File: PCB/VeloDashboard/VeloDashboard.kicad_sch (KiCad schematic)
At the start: 1 part

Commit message: Teensy & LDD & Led strips
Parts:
- added C1: 22nF, symbol Device:C_Polarized
- added IC1, IC2, IC3, IC4: LDD-700L, LDD-XXXL, symbol LDD-700L:LDD-700L
- added R1, R2, R3, R4: 47k, symbol Device:R
- added U1: SN74AHCT125N, digikey-footprints:DIP-14_W3mm, symbol dk_Logic-Buffers-Drivers-Receivers-Transceivers:SN74AHCT125N
- added U2: LC78_05 2.0, Package_TO_SOT_THT:TO-220-3_Vertical, symbol Regulator_Linear:LM7805_TO220
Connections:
- net LED front L: now reaches U?.10 (8_TX2_IN1)
- net LED front L: now also IC1.3 (PWMDIM), R1.2
- net LED front R: now reaches U?.11 (9_OUT1C)
- net LED front R: now also IC2.3 (PWMDIM), R2.2
- net LED rear: now reaches U?.12 (10_CS_MQSR)
- net LED rear: now also IC3.3 (PWMDIM), R3.2
- net LED break: now reaches U?.13 (11_MOSI_CTX1)
- net LED break: now also IC4.3 (PWMDIM), R4.2
- net at U?.4 (2_OUT2): now also U1.2 (1A)
- net at U?.5 (3_LRCLK2): now also U1.5 (2A)
- new net +12V: IC1.1 (+VIN), IC2.1 (+VIN), IC3.1 (+VIN), IC4.1 (+VIN), U2.1 (VI)
- new net +5V: C1.1, U1.14 (VCC), U2.3 (VO)
- new net BREAK +: IC4.6 (+VOUT)
- new net BREAK -: IC4.5 (-VOUT)
- new net FRONT LEFT +: IC1.6 (+VOUT)
- new net FRONT LEFT -: IC1.5 (-VOUT)
- new net FRONT RIGHT +: IC2.6 (+VOUT)
- new net FRONT RIGHT -: IC2.5 (-VOUT)
- new net GND: C1.2, R1.1, R2.1, R3.1, R4.1, U1.1 (1~{OE}), U1.4 (2~{OE}), U1.7 (GND), U2.2 (GND)
- new net GND1: IC1.4 (-VIN), IC2.4 (-VIN), IC3.4 (-VIN), IC4.4 (-VIN)
- new net LED strip L: U1.3 (1Y)
- new net LED strip R: U1.6 (2Y)
- new net REAR +: IC3.6 (+VOUT)
- new net REAR -: IC3.5 (-VOUT)
- no-connect marks 0 -> 6
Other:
- moved on the sheet: U?

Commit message: Power & Dashboard & OLED & others
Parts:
- added BT1: Battery Cell 3.3V, symbol Device:Battery_Cell
- added J1: Speed Sensor, symbol Connector:Conn_01x02_Pin
- added J1.in: ~, symbol Connector:Conn_01x07_Pin
- added J1.out: Polulu Power, symbol Connector:Conn_01x06_Pin
- added J2: OLED 128 x 64, symbol Connector:Conn_01x04_Pin
- added R10: 20k, symbol Device:R
- added R11, R12: 2.2k, symbol Device:R
- added R13, R8: 3.3k, symbol Device:R
- added R5: 4M, symbol Device:R
- added R6: 1M, symbol Device:R
- added R7: 10K, symbol Device:R
- added R9: 10k, symbol Device:R
- added SW1: On / Off switch, symbol Switch:SW_Push
- added SW2: Down (lights), symbol Switch:SW_Push
- added SW3: Left, symbol Switch:SW_Push
- added SW4: Up (lights), symbol Switch:SW_Push
- added SW5: Horn, symbol Switch:SW_Push
- added SW6: Display, symbol Switch:SW_Push
- added SW7: Right, symbol Switch:SW_Push
- added SW8: Brake, symbol Switch:SW_Push
- C1: value 22nF -> 22µF
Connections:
- net +12V: now also J1.out.1 (Pin_1), J1.out.2 (Pin_2), R5.1
- net +5V: now also U?.33 (VIN)
- net GND: now also U?.1 (GND), BT1.2 (-), J1.2 (Pin_2), J1.out.3 (Pin_3), J1.out.4 (Pin_4), R11.2, R6.2
- net at U?.15 (VBAT): now also BT1.1 (+)
- net at U?.25 (18_A4_SDA0): now also J2.3 (Pin_3)
- net at U?.26 (19_A5_SCL0): now also J2.4 (Pin_4)
- net at U?.29 (22_A8_CTX1): now also R7.1, SW2.1, SW3.1, SW4.1, SW5.1, SW6.1, SW7.1, SW8.1
- net Power meter: now reaches U?.30 (23_A9_CRX1_MCLK1)
- net Power meter: now also R5.2, R6.1
- net at U?.31 (3V3): now also J2.1 (Pin_1), R7.2
- net at U?.32 (GND): now also J2.2 (Pin_2)
- net at U?.6 (4_BCLK2): now also J1.1 (Pin_1)
- net Power OFF: now reaches U?.7 (5_IN2)
- net Power OFF: now also J1.in.6 (Pin_6)
- new net: R11.1, R12.1, SW5.2
- new net: R12.2, R13.1, SW6.2
- new net: R13.2, R8.1, SW7.2, SW8.2
- new net: R10.2, SW4.2
- new net: R10.1, R9.2, SW2.2
- new net: R8.2, R9.1, SW3.2
- new net: J1.out.5 (Pin_5), SW1.2
- new net: J1.out.6 (Pin_6), SW1.1
- new net ACCU + (11.1 V LiPo): J1.in.1 (Pin_1), J1.in.2 (Pin_2)
- new net ACCU -: J1.in.3 (Pin_3), J1.in.4 (Pin_4)
- no-connect marks 6 -> 41
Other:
- note added: "Dashboard Buttons"
- note added: "Power"
- moved on the sheet: C1, U2

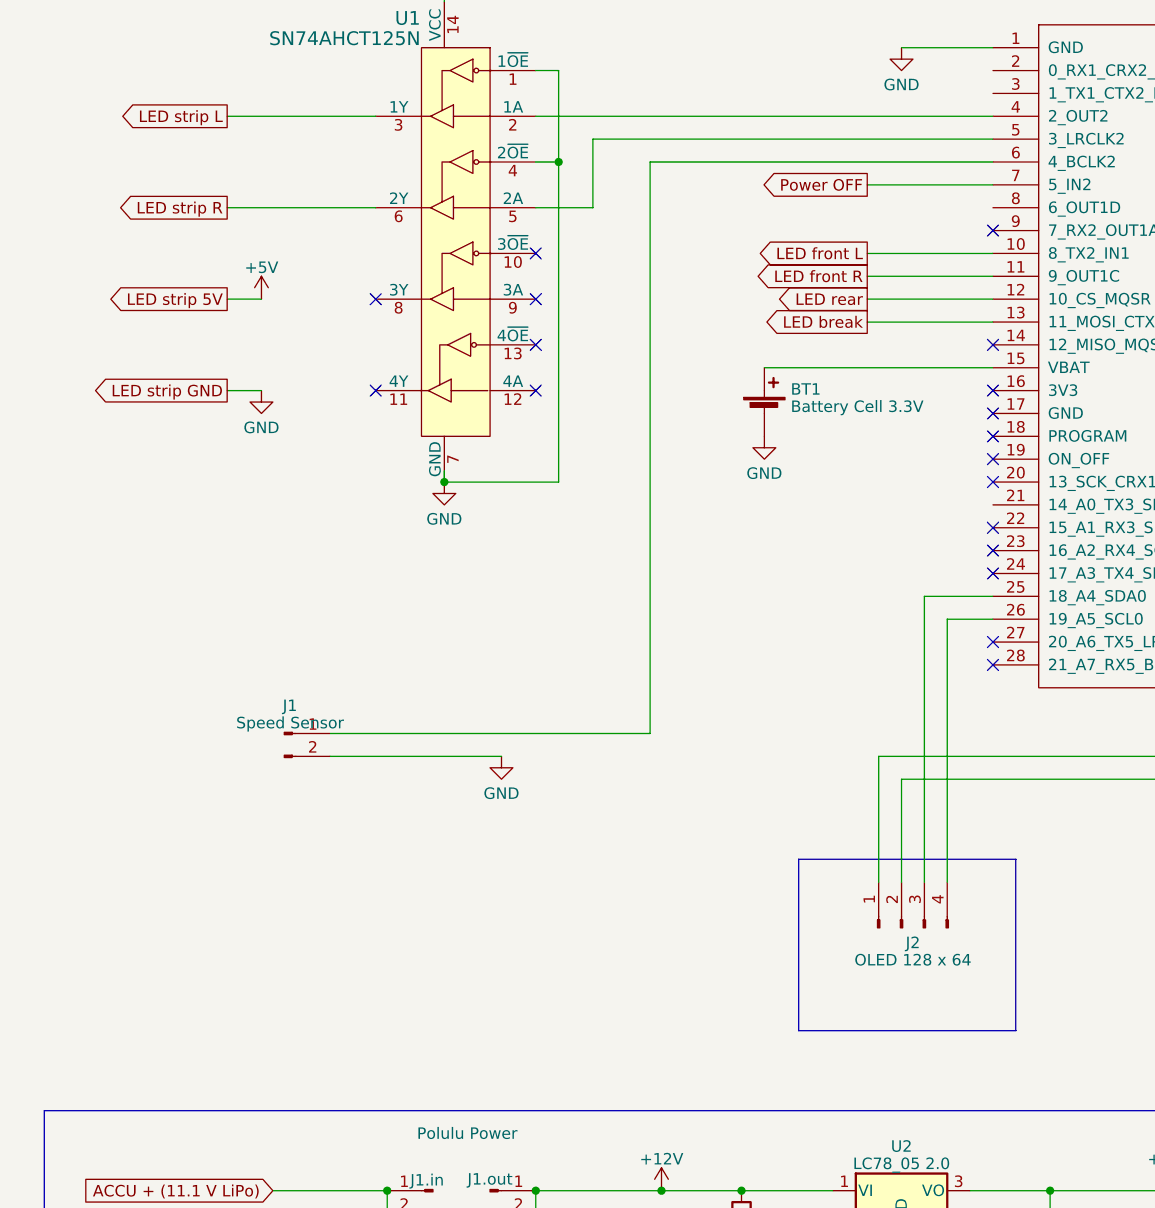
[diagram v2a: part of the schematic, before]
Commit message: buzzer with mosfet added
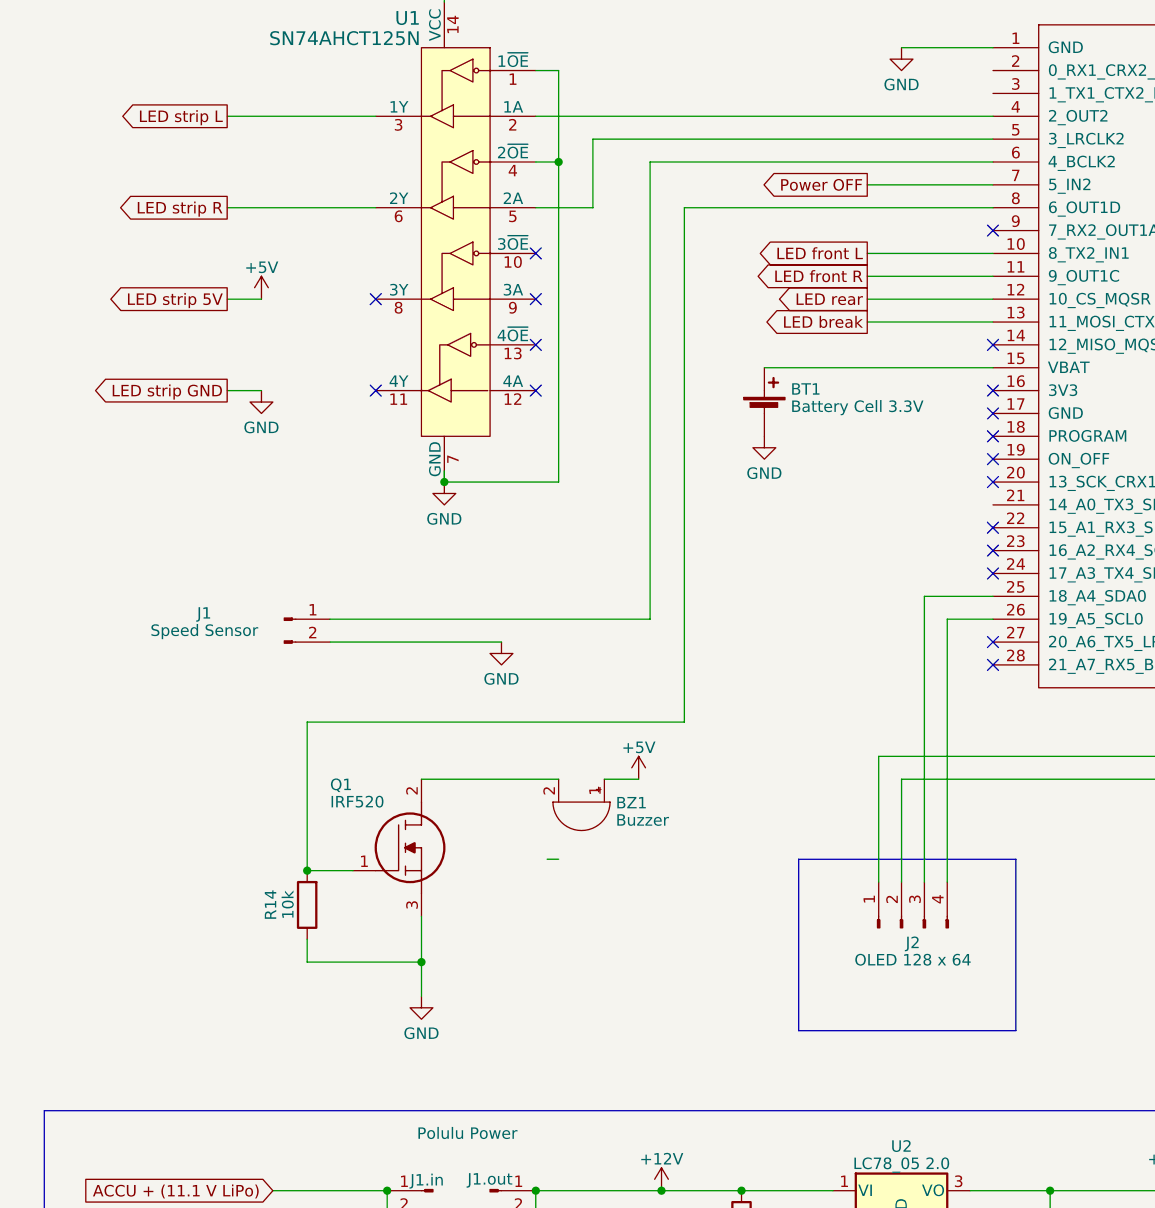
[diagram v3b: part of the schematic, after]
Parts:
- added BZ1: Buzzer, symbol Device:Buzzer
- added Q1: IRF520, TO270P460X1020X2008-3P, symbol IRF520:IRF520
- added R14: 10k, symbol Device:R
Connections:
- net +5V: now also BZ1.1 (-)
- net GND: now also Q1.3, R14.1
- net at U?.8 (6_OUT1D): now also Q1.1, R14.2
- new net: BZ1.2 (+), Q1.2
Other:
- moved on the sheet: J1

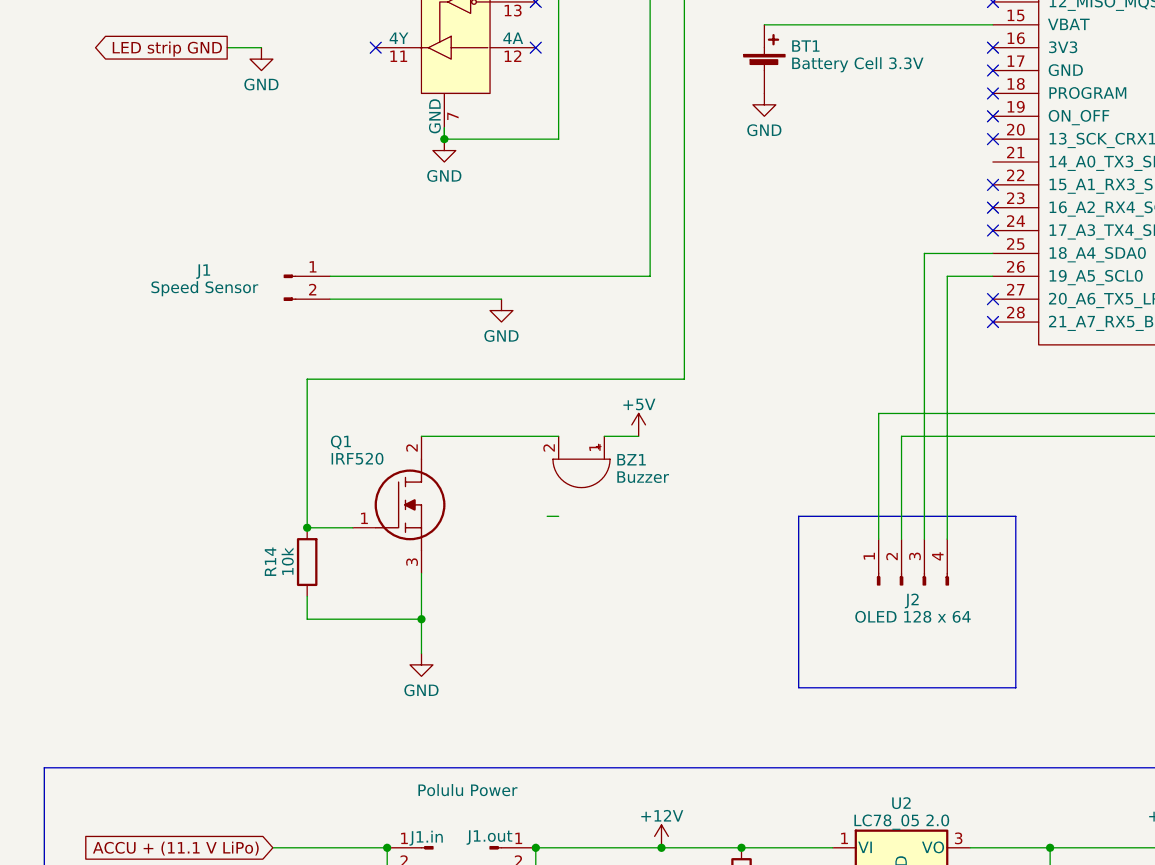
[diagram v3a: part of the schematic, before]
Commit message: Toeter & Relay toegevoegd
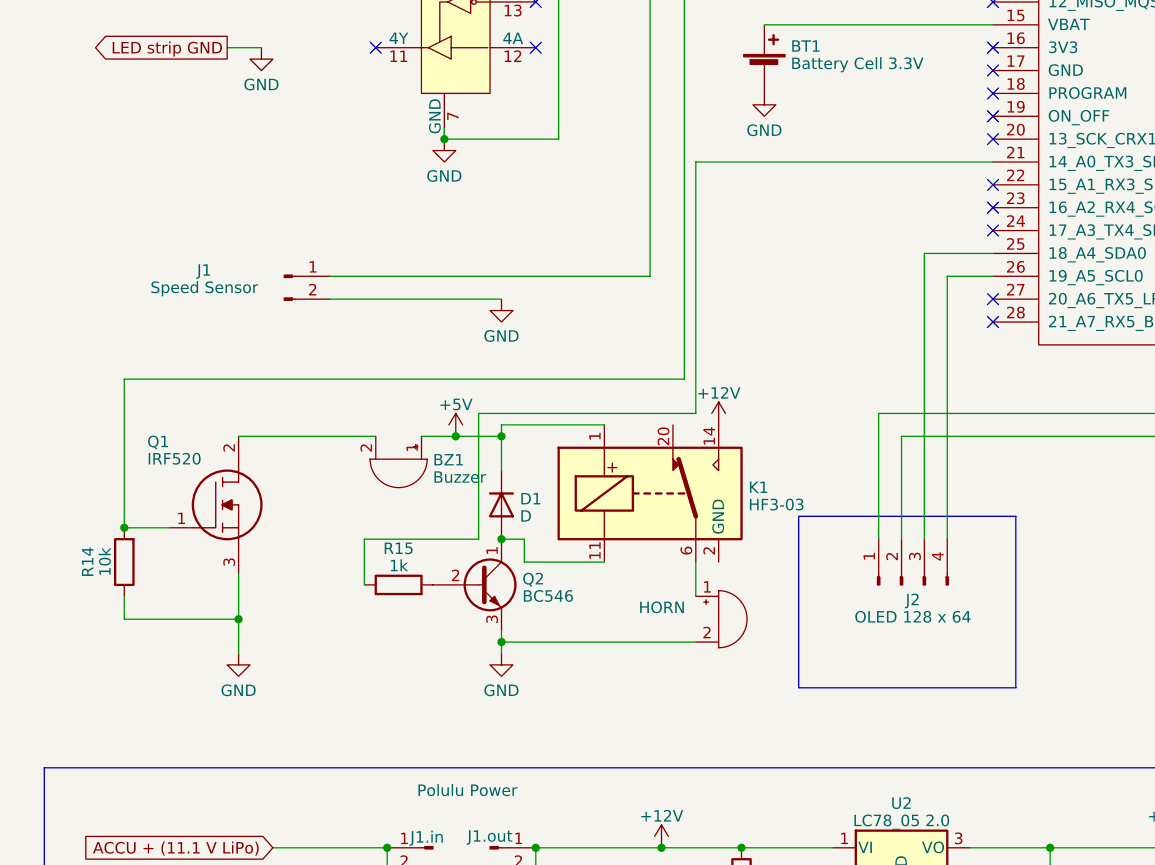
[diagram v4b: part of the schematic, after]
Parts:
- added D1: D, symbol Device:D
- added HORN: (no value), symbol Device:Buzzer
- added K1: HF3-03, Relay_SMD:Relay_SPDT_AXICOM_HF3Series_75ohms_Pitch1.27mm, symbol Relay:HF3-03
- added Q2: BC546, Package_TO_SOT_THT:TO-92_Inline, symbol Transistor_BJT:BC546
- added R15: 1k, symbol Device:R
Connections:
- net +12V: now also K1.14
- net +5V: now also D1.1 (K), K1.1
- net GND: now also HORN.2 (+), Q2.3 (E)
- net at U?.21 (14_A0_TX3_SPDIF_OUT): now also R15.1
- new net: Q2.2 (B), R15.2
- new net: D1.2 (A), K1.11, Q2.1 (C)
- new net: HORN.1 (-), K1.6
- new net: K1.10 (GND), K1.12 (GND), K1.13 (GND), K1.15 (GND), K1.17 (GND), K1.19 (GND), K1.2 (GND), K1.21 (GND), K1.22 (GND), K1.5 (GND), K1.7 (GND)
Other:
- moved on the sheet: BZ1, Q1, R14

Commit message: updatet schematics
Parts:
- added D2: LEFT, symbol Device:LED
- added D3: RIGHT, symbol Device:LED
- added D4: BRAKE, symbol Device:LED
- added J3, J4: RJ32, symbol Connector:RJ32
- added R16, R17: 220, symbol Device:R
- added R18, R19, R20, R21: 220k, symbol Device:R
- HORN: value (none) -> ~
- R10: value 20k -> 100k
- R11: value 2.2k -> 220k
- R12: value 2.2k -> 100k
- R13: value 3.3k -> 100k
- R7: value 10K -> 220
- R8: value 3.3k -> 220k
- R9: value 10k -> 100k
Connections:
- net GND: now also R8.1, D2.2 (A), D3.2 (A), D4.2 (A), J4.1, R19.2
- net Power meter: no longer U?.30 (23_A9_CRX1_MCLK1)
- net at U?.23 (16_A2_RX4_SCL1): now also J2.4 (Pin_4)
- net at U?.24 (17_A3_TX4_SDA1): now also J2.3 (Pin_3)
- net at U?.25 (18_A4_SDA0): now also J3.8; no longer J2.3 (Pin_3)
- net at U?.26 (19_A5_SCL0): now also J3.7; no longer J2.4 (Pin_4)
- net at U?.27 (20_A6_TX5_LRCLK1): now also J3.6
- net at U?.28 (21_A7_RX5_BCLK1): now also J3.5
- net at J2.1 (Pin_1), U?.31 (3V3): now also J3.2; no longer R7.2
- net at J2.2 (Pin_2), U?.32 (GND): now also J3.1
- net at R13.2, SW7.2: no longer R8.1, SW8.2
- new net: J3.4, U?.29 (22_A8_CTX1)
- new net: J3.3, U?.30 (23_A9_CRX1_MCLK1)
- new net: D2.1 (K), R7.2
- new net: J4.8, R20.1, SW5.1, SW6.1, SW7.1
- new net: J4.3, R7.1
- new net: J4.7, R21.1, SW2.1, SW3.1, SW4.1
- new net: R19.1, SW8.2
- new net: J4.6, R18.1, SW8.1
- new net: J4.5, R17.1
- new net: D4.1 (K), R17.2
- new net: D3.1 (K), R16.2
- new net: J4.4, R16.1
- new net +3.3V: J4.2, R18.2, R20.2, R21.2
- no-connect marks 41 -> 36
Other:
- note added: "Dashboard connector"
- note removed: "Dashboard Buttons"
- moved on the sheet: R10, R11, R12, R13, R8, R9, SW2, SW3, SW4, SW5, SW6, SW7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
